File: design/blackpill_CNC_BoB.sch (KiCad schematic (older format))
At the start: 288 parts, among them J101 ALimIN, J102 ZLimIN, J103 YLimIN, J104 XLimIN, J105 CS_IN, J106 FH_IN, J107 DoorIN, J108 ResetIN, J109 ProbeIN, J110 12V Power in, J111 AuxEncIn, J112 5V Power out, J113 ADC_in_1, J114 ADC_in_2, J115 stepDriverLim, J116 Reset, J117 UART1, J118 I2C, J119 SpindleVFD, J120 Spindle/Coolant, J121 Spindle, J122 Coolant, J123 AuxOut, J124 XStepDrv, J125 YStepDrv, J126 ZStepDrv, J127 AStepDrv, U101 TLP290-4, U102 TLP290-4, U103 TLP290-4, U104 74LVC2G17, U105 LD1117S50TR_SOT223, U106 LM358, U107 TLV9001, U108 TLV9001, U109 YAAJ_WeAct_BlackPill_Part_Like, U110 TLV9001, U111 TLV9001, U112 74HCT541, U113 74HCT541, U114 74HCT541, U115 ULN2003A, U116 ULN2003A, U117 ULN2003A

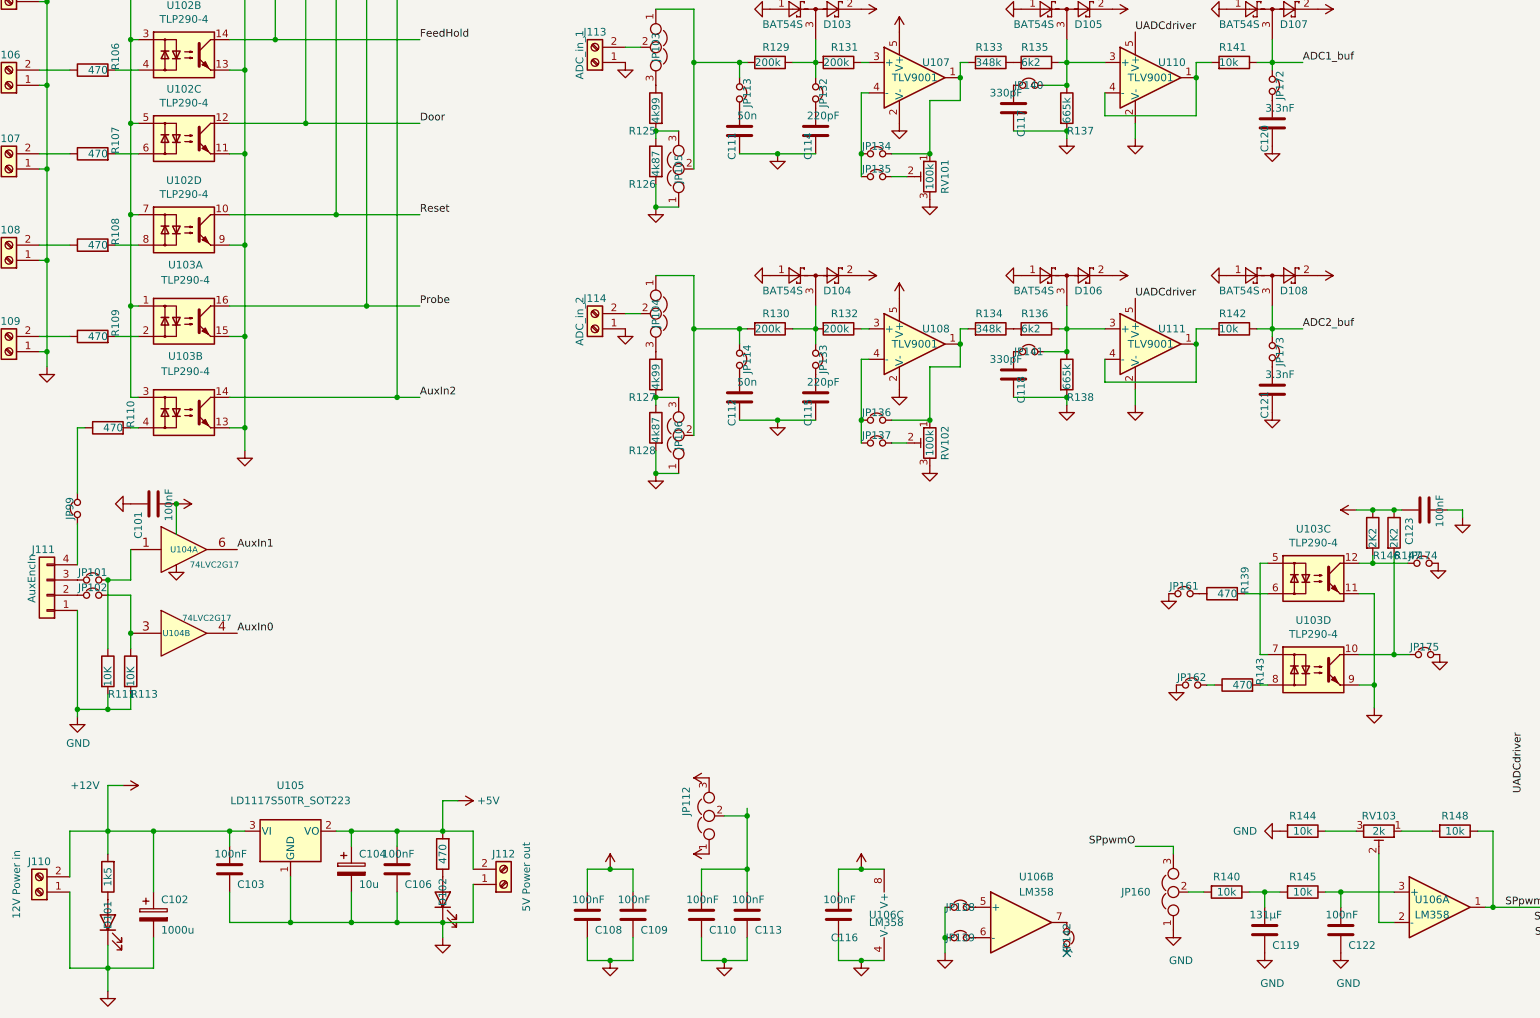
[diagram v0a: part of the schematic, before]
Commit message: JLBPCB tuned capacitors
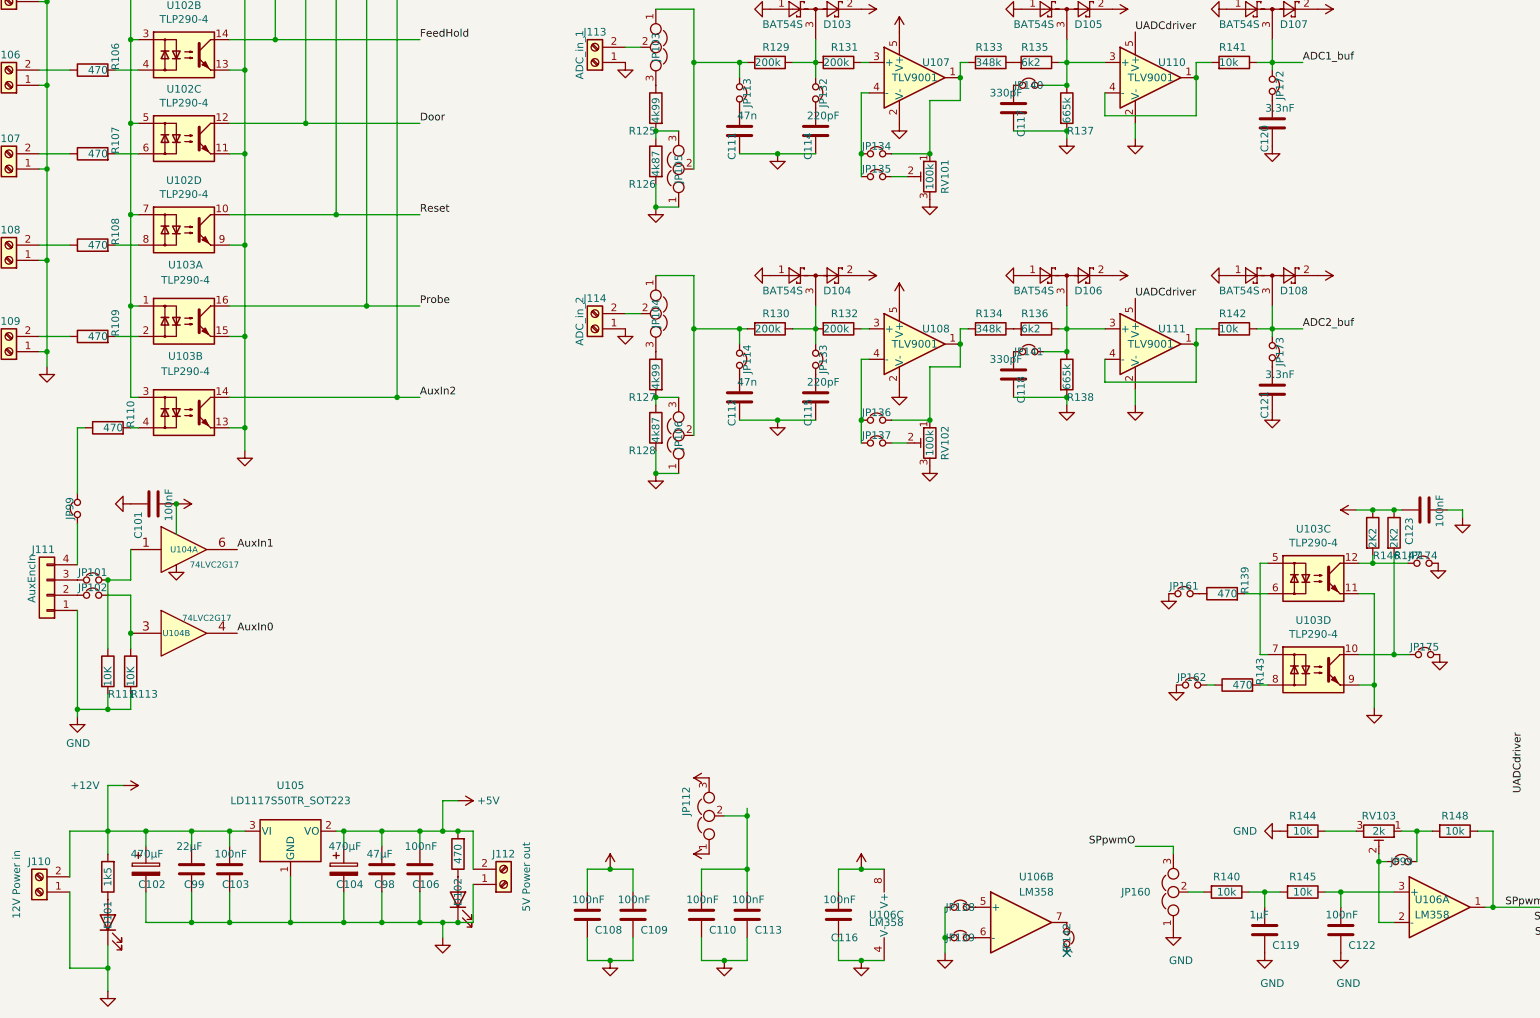
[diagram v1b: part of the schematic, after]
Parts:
- added C98: 47µF, Capacitor_SMD:C_0603_1608Metric, symbol Device:C
- added C99: 22µF, Capacitor_SMD:C_0603_1608Metric, symbol Device:C
- added JP99: Jumper_NC_Small, Connector_PinHeader_2.54mm:PinHeader_1x02_P2.54mm_Vertical, symbol Device:Jumper_NC_Small
- C102: value 1000u -> 470µF
- C104: value 10u -> 470µF
- C111, C112: value 50n -> 47n
- C119: value 131µF -> 1µF
- RV101, RV102, RV103: footprint (none) -> Potentiometer_THT:Potentiometer_Bourns_3296W_Vertical
- U107, U108, U110, U111: footprint Package_TO_SOT_SMD:TSOT-23-5 -> Package_TO_SOT_SMD:SOT-353_SC-70-5
- U109: footprint Kicad-STM32:YAAJ_WeAct_BlackPill2 -> (none)
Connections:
- net +12V: now also C99.1
- net +5V: now also C98.1
- net GND: now also C98.2, C99.2
- net at RV103.2, U106.2 (-): now also JP99.1
- net at R148.2, RV103.1: now also JP99.2
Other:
- moved on the sheet: C102, C104, C106, D102
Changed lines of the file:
@@
 F 0 "U109" H 7050 3360 50  0000 C CNN
 F 1 "YAAJ_WeAct_BlackPill_Part_Like" H 7050 3260 50  0000 C CNN
-F 2 "Kicad-STM32:YAAJ_WeAct_BlackPill2" H 7050 1000 50  0001 C CNN
+F 2 "" H 7050 1000 50  0001 C CNN
 F 3 "" H 7740 1180 50  0001 C CNN
 	1    7040 2180
@@
 F 0 "RV103" V 9650 9850 50  0000 C CNN
 F 1 "2k" V 9750 9850 50  0000 C CNN
-F 2 "" H 9750 9850 50  0001 C CNN
+F 2 "Potentiometer_THT:Potentiometer_Bourns_3296W_Vertical" H 9750 9850 50  0001 C CNN
 F 3 "~" H 9750 9850 50  0001 C CNN
 	1    9750 9850
@@
 P 9000 10500
 F 0 "C119" H 9050 10400 50  0000 L CNN
-F 1 "131µF" H 8900 10600 50  0000 L CNN
+F 1 "1µF" H 8900 10600 50  0000 L CNN
 F 2 "" H 9038 10350 50  0001 C CNN
 F 3 "~" H 9000 10500 50  0001 C CNN
@@
 	10500 10350 11000 10350
 Wire Wire Line
-	10100 9850 9900 9850
+	10100 9850 10000 9850
 Wire Wire Line
 	9850 10450 9750 10450
 Wire Wire Line
-	9750 10450 9750 10000
+	9750 10450 9750 10050
 Wire Wire Line
 	9850 10250 9500 10250
@@
 L Device:R R124
 U 1 1 71ACB987
-P 3600 10000
-F 0 "R124" V 3350 10000 50  0001 C CNN
-F 1 "470" V 3600 10000 50  0000 C CNN
-F 2 "Resistor_SMD:R_0805_2012Metric" V 3530 10000 50  0001 C CNN
-F 3 "~" H 3600 10000 50  0001 C CNN
-	1    3600 10000
+P 3700 10000
+F 0 "R124" V 3450 10000 50  0001 C CNN
+F 1 "470" V 3700 10000 50  0000 C CNN
+F 2 "Resistor_SMD:R_0805_2012Metric" V 3630 10000 50  0001 C CNN
+F 3 "~" H 3700 10000 50  0001 C CNN
+	1    3700 10000
 	-1   0    0    1
 $EndComp
@@
 L Device:LED D102
 U 1 1 71ACB98D
-P 3600 10300
-F 0 "D102" H 3650 10300 50  0000 C CNN
-F 1 "LED" H 3550 10100 50  0001 C CNN
-F 2 "LED_SMD:LED_0805_2012Metric" H 3600 10300 50  0001 C CNN
-F 3 "~" H 3600 10300 50  0001 C CNN
-	1    3600 10300
+P 3700 10300
+F 0 "D102" H 3750 10300 50  0000 C CNN
+F 1 "LED" H 3650 10100 50  0001 C CNN
+F 2 "LED_SMD:LED_0805_2012Metric" H 3700 10300 50  0001 C CNN
+F 3 "~" H 3700 10300 50  0001 C CNN
+	1    3700 10300
 	0    -1   -1   0
 $EndComp
@@
 L Device:CP C102
 U 1 1 71C388FD
-P 1700 10400
-F 0 "C102" H 1750 10500 50  0000 L CNN
-F 1 "1000u" H 1750 10300 50  0000 L CNN
-F 2 "Capacitor_THT:CP_Axial_L29.0mm_D16.0mm_P35.00mm_Horizontal" H 1738 10250 50  0001 C CNN
-F 3 "~" H 1700 10400 50  0001 C CNN
-	1    1700 10400
+P 1650 10100
+F 0 "C102" H 1600 10000 50  0000 L CNN
+F 1 "470µF" H 1550 10200 50  0000 L CNN
+F 2 "Capacitor_THT:CP_Axial_L29.0mm_D16.0mm_P35.00mm_Horizontal" H 1688 9950 50  0001 C CNN
+F 3 "~" H 1650 10100 50  0001 C CNN
+	1    1650 10100
 	1    0    0    -1
 $EndComp
@@
 U 1 1 71C38ECB
 P 2200 10100
-F 0 "C103" H 2250 10000 50  0000 L CNN
+F 0 "C103" H 2150 10000 50  0000 L CNN
 F 1 "100nF" H 2100 10200 50  0000 L CNN
 F 2 "Capacitor_SMD:C_0603_1608Metric" H 2238 9950 50  0001 C CNN
@@
 L Device:CP C104
 U 1 1 71C3928B
-P 3000 10100
-F 0 "C104" H 3050 10200 50  0000 L CNN
-F 1 "10u" H 3050 10000 50  0000 L CNN
-F 2 "Capacitor_SMD:C_1206_3216Metric" H 3038 9950 50  0001 C CNN
-F 3 "~" H 3000 10100 50  0001 C CNN
-	1    3000 10100
+P 2950 10100
+F 0 "C104" H 2900 10000 50  0000 L CNN
+F 1 "470µF" H 2850 10250 50  0000 L CNN
+F 2 "Capacitor_SMD:C_1206_3216Metric" H 2988 9950 50  0001 C CNN
+F 3 "~" H 2950 10100 50  0001 C CNN
+	1    2950 10100
 	1    0    0    -1
 $EndComp
@@
 L Device:C C106
 U 1 1 71D003FD
-P 3300 10100
-F 0 "C106" H 3350 10000 50  0000 L CNN
-F 1 "100nF" H 3200 10200 50  0000 L CNN
-F 2 "Capacitor_SMD:C_0603_1608Metric" H 3338 9950 50  0001 C CNN
-F 3 "~" H 3300 10100 50  0001 C CNN
-	1    3300 10100
+P 3450 10100
+F 0 "C106" H 3400 10000 50  0000 L CNN
+F 1 "100nF" H 3350 10250 50  0000 L CNN
+F 2 "Capacitor_SMD:C_0603_1608Metric" H 3488 9950 50  0001 C CNN
+F 3 "~" H 3450 10100 50  0001 C CNN
+	1    3450 10100
 	1    0    0    -1
 $EndComp
@@
 	2200 9950 2200 9850
 Connection ~ 2200 9850
-Wire Wire Line
-	3600 10450 3300 10450
-Wire Wire Line
-	2900 9850 3000 9850
 Connection ~ 3600 9850
 Wire Wire Line
@@
 Connection ~ 3600 10450
 Wire Wire Line
-	3300 10250 3300 10450
-Connection ~ 3300 10450
-Wire Wire Line
-	3300 10450 3000 10450
-Wire Wire Line
-	3000 10250 3000 10450
-Connection ~ 3000 10450
-Wire Wire Line
-	3000 10450 2600 10450
-Wire Wire Line
 	2600 10150 2600 10450
 Connection ~ 2600 10450
@@
 	2200 10250 2200 10450
 Wire Wire Line
-	3000 9950 3000 9850
-Connection ~ 3000 9850
-Wire Wire Line
-	3000 9850 3300 9850
-Wire Wire Line
-	3300 9950 3300 9850
-Connection ~ 3300 9850
-Wire Wire Line
-	3300 9850 3600 9850
-Wire Wire Line
 	1500 9550 1400 9550
 Wire Wire Line
@@
 	3600 9650 3600 9850
 Wire Wire Line
-	1400 9850 1700 9850
-Wire Wire Line
 	1400 10600 1400 10750
-Wire Wire Line
-	1700 10550 1700 10750
-Wire Wire Line
-	1700 10750 1400 10750
 Connection ~ 1400 10750
 Wire Wire Line
 	1400 10750 1400 10900
-Wire Wire Line
-	1700 10250 1700 9850
-Connection ~ 1700 9850
-Wire Wire Line
-	1700 9850 2200 9850
 $Comp
 L power:+3.3V #PWR0107
@@
 	3800 10100 3800 9850
 Wire Wire Line
-	3800 9850 3600 9850
+	3800 9850 3700 9850
 Wire Wire Line
 	3800 10200 3800 10450
 Wire Wire Line
-	3800 10450 3600 10450
+	3800 10450 3700 10450
 $Comp
 L Device:C C107
@@
 P 5550 5250
 F 0 "C111" V 5600 5150 50  0000 C CNN
-F 1 "50n" H 5500 5350 50  0000 C CNN
+F 1 "47n" H 5500 5350 50  0000 C CNN
 F 2 "Capacitor_SMD:C_0603_1608Metric" H 5588 5100 50  0001 C CNN
 F 3 "~" H 5550 5250 50  0001 C CNN
@@
 F 0 "RV101" V 6700 5550 50  0000 C CNN
 F 1 "100k" V 6800 5550 50  0000 C CNN
-F 2 "" H 6800 5550 50  0001 C CNN
+F 2 "Potentiometer_THT:Potentiometer_Bourns_3296W_Vertical" H 6800 5550 50  0001 C CNN
 F 3 "~" H 6800 5550 50  0001 C CNN
 	1    6800 5550
@@
 F 0 "U110" H 8300 5000 50  0000 L CNN
 F 1 "TLV9001" H 8100 4900 50  0000 L CNN
-F 2 "Package_TO_SOT_SMD:TSOT-23-5" H 8250 4900 50  0001 C CNN
+F 2 "Package_TO_SOT_SMD:SOT-353_SC-70-5" H 8250 4900 50  0001 C CNN
 F 3 "http://www.analog.com/media/en/technical-documentation/data-sheets/AD8603_8607_8609.pdf" H 8250 5100 50  0001 C CNN
 	1    8250 4900
@@
 F 0 "U107" H 6750 5000 50  0000 L CNN
 F 1 "TLV9001" H 6550 4900 50  0000 L CNN
-F 2 "Package_TO_SOT_SMD:TSOT-23-5" H 6700 4900 50  0001 C CNN
+F 2 "Package_TO_SOT_SMD:SOT-353_SC-70-5" H 6700 4900 50  0001 C CNN
 F 3 "http://www.analog.com/media/en/technical-documentation/data-sheets/AD8603_8607_8609.pdf" H 6700 5100 50  0001 C CNN
 	1    6700 4900
@@
 P 5550 7000
 F 0 "C112" V 5600 6900 50  0000 C CNN
-F 1 "50n" H 5500 7100 50  0000 C CNN
+F 1 "47n" H 5500 7100 50  0000 C CNN
 F 2 "Capacitor_SMD:C_0603_1608Metric" H 5588 6850 50  0001 C CNN
 F 3 "~" H 5550 7000 50  0001 C CNN
@@
 F 0 "RV102" V 6700 7300 50  0000 C CNN
 F 1 "100k" V 6800 7300 50  0000 C CNN
-F 2 "" H 6800 7300 50  0001 C CNN
+F 2 "Potentiometer_THT:Potentiometer_Bourns_3296W_Vertical" H 6800 7300 50  0001 C CNN
 F 3 "~" H 6800 7300 50  0001 C CNN
 	1    6800 7300
@@
 F 0 "U111" H 8300 6750 50  0000 L CNN
 F 1 "TLV9001" H 8100 6650 50  0000 L CNN
-F 2 "Package_TO_SOT_SMD:TSOT-23-5" H 8250 6650 50  0001 C CNN
+F 2 "Package_TO_SOT_SMD:SOT-353_SC-70-5" H 8250 6650 50  0001 C CNN
 F 3 "http://www.analog.com/media/en/technical-documentation/data-sheets/AD8603_8607_8609.pdf" H 8250 6850 50  0001 C CNN
 	1    8250 6650
@@
 F 0 "U108" H 6750 6750 50  0000 L CNN
 F 1 "TLV9001" H 6550 6650 50  0000 L CNN
-F 2 "Package_TO_SOT_SMD:TSOT-23-5" H 6700 6650 50  0001 C CNN
+F 2 "Package_TO_SOT_SMD:SOT-353_SC-70-5" H 6700 6650 50  0001 C CNN
 F 3 "http://www.analog.com/media/en/technical-documentation/data-sheets/AD8603_8607_8609.pdf" H 6700 6850 50  0001 C CNN
 	1    6700 6650
@@
 Wire Wire Line
 	1200 7830 1200 8100
+$Comp
+L Device:Jumper_NC_Small JP99
+U 1 1 66C69E3B
+P 9900 10050
+F 0 "JP99" H 9900 10050 50  0000 C CNN
+F 1 "Jumper_NC_Small" H 9900 10200 50  0001 C CNN
+F 2 "Connector_PinHeader_2.54mm:PinHeader_1x02_P2.54mm_Vertical" H 9900 10050 50  0001 C CNN
+F 3 "~" H 9900 10050 50  0001 C CNN
+	1    9900 10050
+	1    0    0    -1
+$EndComp
+Wire Wire Line
+	9800 10050 9750 10050
+Connection ~ 9750 10050
+Wire Wire Line
+	9750 10050 9750 10000
+Wire Wire Line
+	10000 10050 10000 9850
+Connection ~ 10000 9850
+Wire Wire Line
+	10000 9850 9900 9850
+Wire Wire Line
+	1400 9850 1650 9850
+$Comp
+L Device:C C99
+U 1 1 66D5FDC1
+P 1950 10100
+F 0 "C99" H 1900 10000 50  0000 L CNN
+F 1 "22µF" H 1850 10250 50  0000 L CNN
+F 2 "Capacitor_SMD:C_0603_1608Metric" H 1988 9950 50  0001 C CNN
+F 3 "~" H 1950 10100 50  0001 C CNN
+	1    1950 10100
+	1    0    0    -1
+$EndComp
+Wire Wire Line
+	2900 9850 2950 9850
+Wire Wire Line
+	2600 10450 2950 10450
+Connection ~ 3700 9850
+Wire Wire Line
+	3700 9850 3600 9850
+Connection ~ 3700 10450
+Wire Wire Line
+	3700 10450 3600 10450
+$Comp
+L Device:C C98
+U 1 1 66DD83EF
+P 3200 10100
+F 0 "C98" H 3150 10000 50  0000 L CNN
+F 1 "47µF" H 3100 10200 50  0000 L CNN
+F 2 "Capacitor_SMD:C_0603_1608Metric" H 3238 9950 50  0001 C CNN
+F 3 "~" H 3200 10100 50  0001 C CNN
+	1    3200 10100
+	1    0    0    -1
+$EndComp
+Wire Wire Line
+	2200 10450 1950 10450
+Wire Wire Line
+	1650 10450 1650 10250
+Connection ~ 2200 10450
+Wire Wire Line
+	1650 9950 1650 9850
+Connection ~ 1650 9850
+Wire Wire Line
+	1650 9850 1950 9850
+Wire Wire Line
+	1950 9950 1950 9850
+Connection ~ 1950 9850
+Wire Wire Line
+	1950 9850 2200 9850
+Wire Wire Line
+	1950 10250 1950 10450
+Connection ~ 1950 10450
+Wire Wire Line
+	1950 10450 1650 10450
+Wire Wire Line
+	2950 10250 2950 10450
+Connection ~ 2950 10450
+Wire Wire Line
+	2950 10450 3200 10450
+Wire Wire Line
+	3200 10250 3200 10450
+Connection ~ 3200 10450
+Wire Wire Line
+	3200 10450 3450 10450
+Wire Wire Line
+	3450 10250 3450 10450
+Connection ~ 3450 10450
+Wire Wire Line
+	3450 10450 3600 10450
+Wire Wire Line
+	3450 9950 3450 9850
+Connection ~ 3450 9850
+Wire Wire Line
+	3450 9850 3600 9850
+Wire Wire Line
+	3200 9950 3200 9850
+Connection ~ 3200 9850
+Wire Wire Line
+	3200 9850 3450 9850
+Wire Wire Line
+	2950 9950 2950 9850
+Connection ~ 2950 9850
+Wire Wire Line
+	2950 9850 3200 9850
 $EndSCHEMATC
